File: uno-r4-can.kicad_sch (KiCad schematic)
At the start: 17 parts, among them J101 CANOpen, J102 Power, J103 Analog, J104 Digital/PWM, J105 Digital/PWM, U1 L78L05_SOT89, U2 ISO1050DUB

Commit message: Printable docs for schematic and model
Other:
- title: (none) -> Arduino Uno R4 CAN Shield
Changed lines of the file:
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@@
   (paper "A4")
   (title_block
+    (title "Arduino Uno R4 CAN Shield")
     (date "2023-10-29")
+    (rev "0.1")
   )
   (junction (at 44.45 119.38) (diameter 0) (color 0 0 0 0)

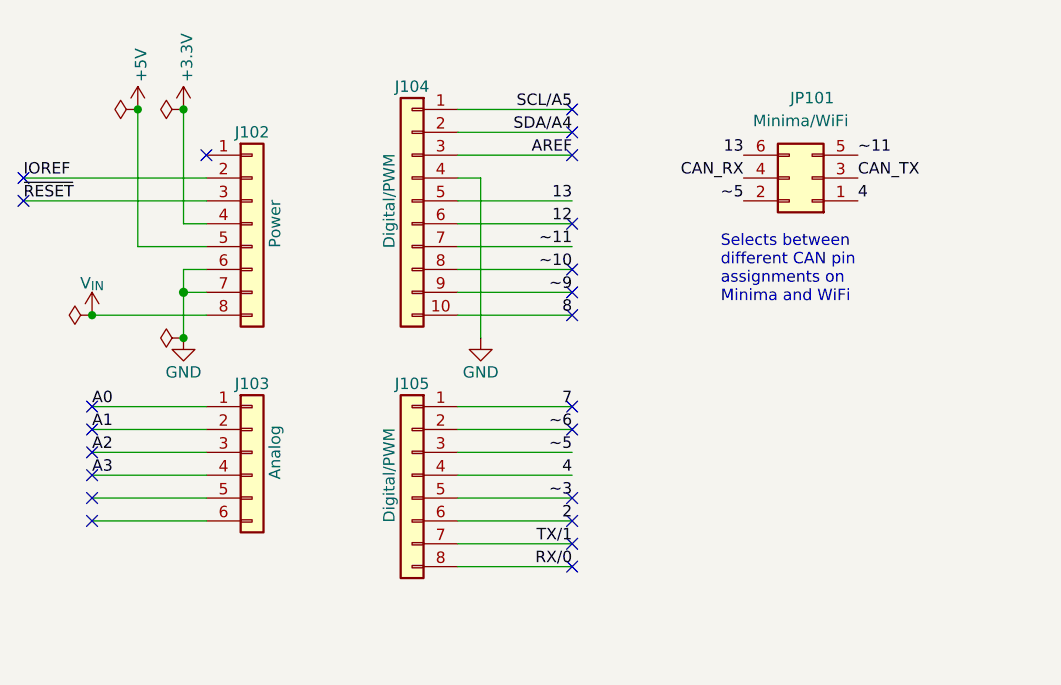
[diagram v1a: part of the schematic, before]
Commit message: Wifi TX is on pin 10
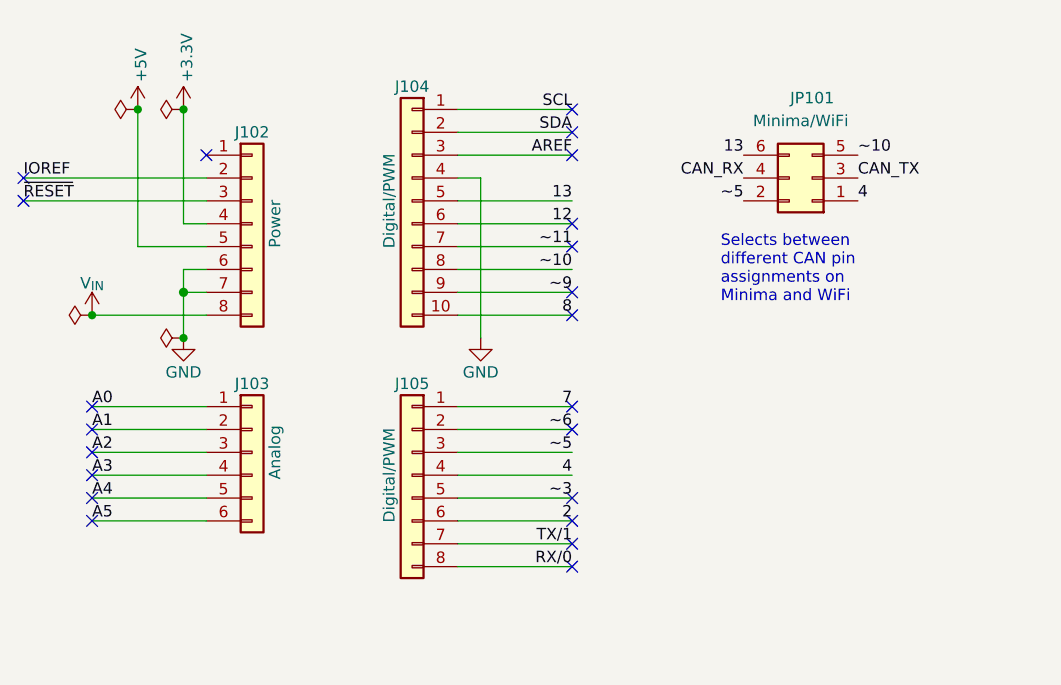
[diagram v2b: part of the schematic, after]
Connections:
- net ~10: now also JP101.5 (Pin_5)
- net ~11: no longer JP101.5 (Pin_5)
- net A4: now reaches J103.5 (Pin_5)
- net A5: now reaches J103.6 (Pin_6)
- net SCL/A5 renamed SCL
- net SDA/A4 renamed SDA
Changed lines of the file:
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@@
   (no_connect (at 86.36 77.47))
   (no_connect (at 86.36 59.69))
-  (no_connect (at 86.36 44.45))
+  (no_connect (at 86.36 41.91))
   (no_connect (at 33.02 64.77))
   (no_connect (at 33.02 62.23))
@@
     (effects (font (size 1.27 1.27)) (justify right bottom))
   )
+  (label "A5" (at 33.02 72.39 0) (fields_autoplaced)
+    (effects (font (size 1.27 1.27)) (justify left bottom))
+  )
   (label "2" (at 86.36 72.39 180) (fields_autoplaced)
     (effects (font (size 1.27 1.27)) (justify right bottom))
@@
     (effects (font (size 1.27 1.27)) (justify right bottom))
   )
-  (label "SDA{slash}A4" (at 86.36 29.21 180) (fields_autoplaced)
+  (label "SDA" (at 86.36 29.21 180) (fields_autoplaced)
     (effects (font (size 1.27 1.27)) (justify right bottom))
   )
@@
     (effects (font (size 1.27 1.27)) (justify right bottom))
   )
-  (label "~11" (at 118.11 31.75 0) (fields_autoplaced)
+  (label "~10" (at 118.11 31.75 0) (fields_autoplaced)
     (effects (font (size 1.27 1.27)) (justify left bottom))
   )
@@
     (effects (font (size 1.27 1.27)) (justify right bottom))
   )
-  (label "SCL{slash}A5" (at 86.36 26.67 180) (fields_autoplaced)
-    (effects (font (size 1.27 1.27)) (justify right bottom))
-  )
+  (label "A4" (at 33.02 69.85 0) (fields_autoplaced)
+    (effects (font (size 1.27 1.27)) (justify left bottom))
+  )
+  (label "SCL" (at 86.36 26.67 180) (fields_autoplaced)
+    (effects (font (size 1.27 1.27)) (justify right bottom))
+  )
